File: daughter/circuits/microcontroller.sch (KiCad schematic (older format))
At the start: 17 parts, among them U13 ESP32-WROOM-32, U14 Si7020-A20

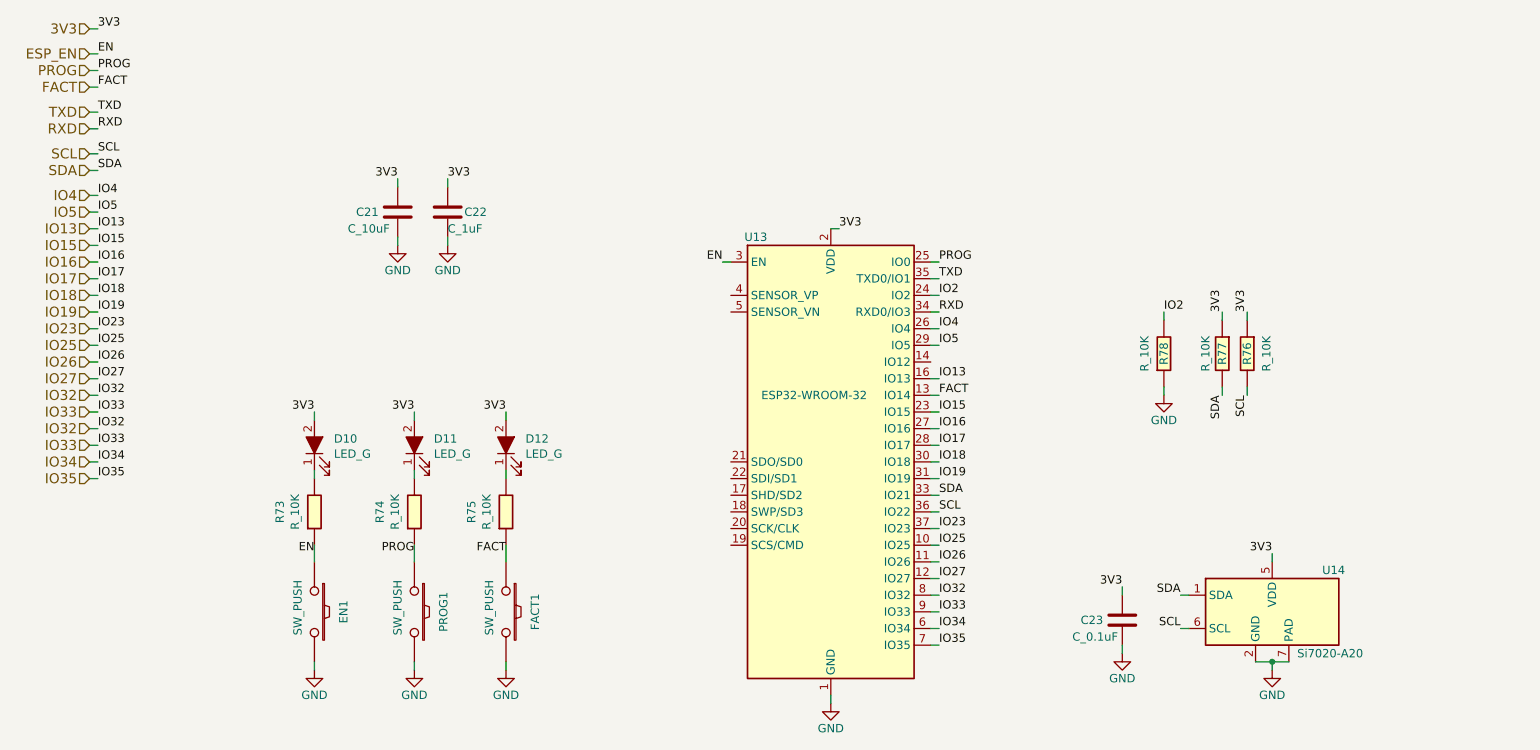
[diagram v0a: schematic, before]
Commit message: 0) Switched to h-bridge drivers for hvac 1) Connected ignition sense io 2) MCP config pins and reset 3) Fixed usb resistors 4) Fixed BJT footprint 5) Added car interface pcb for C6 Corvette
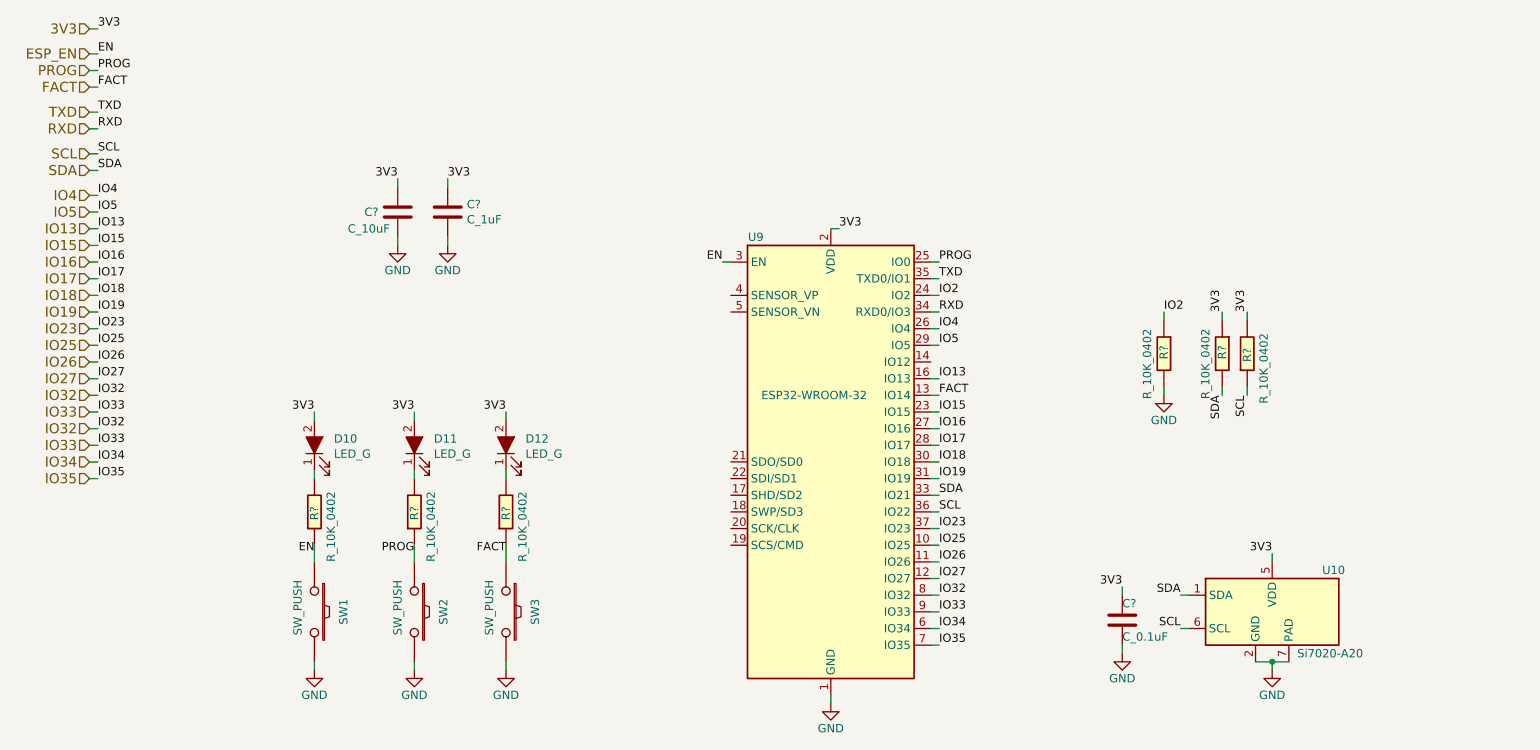
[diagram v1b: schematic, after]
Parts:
- removed C21: C_10uF, Capacitor_SMD:C_0603_1608Metric_Pad1.08x0.95mm_HandSolder, symbol open-dash-daughterboard-rescue:C_10uF-Open_Automation
- removed C22: C_1uF, Capacitor_SMD:C_0603_1608Metric_Pad1.08x0.95mm_HandSolder, symbol open-dash-daughterboard-rescue:C_1uF-Open_Automation
- removed C23: C_0.1uF, Capacitor_SMD:C_0603_1608Metric_Pad1.08x0.95mm_HandSolder, symbol open-dash-daughterboard-rescue:C_0.1uF-Open_Automation
- removed R73, R74, R75, R76, R77, R78: R_10K, Resistor_SMD:R_0603_1608Metric_Pad0.98x0.95mm_HandSolder, symbol open-dash-daughterboard-rescue:R_10K-Open_Automation
- removed U13: ESP32-WROOM-32, RF_Module:ESP32-WROOM-32, symbol open-dash-daughterboard-rescue:ESP32-WROOM-32-Open_Automation
- added C?: C_10uF, Capacitor_SMD:C_0805_2012Metric_Pad1.18x1.45mm_HandSolder, symbol Open_Automation:C_10uF
- added C?: C_1uF, Capacitor_SMD:C_0402_1005Metric_Pad0.74x0.62mm_HandSolder, symbol Open_Automation:C_1uF
- added C?: C_0.1uF, Capacitor_SMD:C_0402_1005Metric_Pad0.74x0.62mm_HandSolder, symbol Open_Automation:C_0.1uF
- added R? (x6): R_10K_0402, Resistor_SMD:R_0402_1005Metric_Pad0.72x0.64mm_HandSolder, symbol Open_Automation:R_10K_0402
- added U9: ESP32-WROOM-32, RF_Module:ESP32-WROOM-32, symbol open-dash-daughterboard-rescue:ESP32-WROOM-32-Open_Automation
- renumbered EN1 to SW1, PROG1 to SW2, FACT1 to SW3, U14 to U10
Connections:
- net 3V3: now also C?.1, C?.1, C?.1, R?.1, R?.2, U9.2 (VDD)
- net ESP_EN: now also R?.1, U9.3 (EN)
- net FACT: now also R?.1, U9.13 (IO14)
- net GND: now also C?.2, C?.2, C?.2, R?.2, U9.1 (GND), U9.15 (GND), U9.38 (GND), U9.39 (GND)
- net IO13: now also U9.16 (IO13)
- net IO15: now also U9.23 (IO15)
- net IO16: now also U9.27 (IO16)
- net IO17: now also U9.28 (IO17)
- net IO18: now also U9.30 (IO18)
- net IO19: now also U9.31 (IO19)
- net IO2: now also R?.1, U9.24 (IO2)
- net IO23: now also U9.37 (IO23)
- net IO25: now also U9.10 (IO25)
- net IO26: now also U9.11 (IO26)
- net IO27: now also U9.12 (IO27)
- net IO32: now also U9.8 (IO32)
- net IO33: now also U9.9 (IO33)
- net IO34: now also U9.6 (IO34)
- net IO35: now also U9.7 (IO35)
- net IO4: now also U9.26 (IO4)
- net IO5: now also U9.29 (IO5)
- net PROG: now also R?.1, U9.25 (IO0)
- net RXD: now also U9.34 (RXD0/IO3)
- net SCL: now also R?.1, U9.36 (IO22)
- net SDA: now also R?.2, U9.33 (IO21)
- net TXD: now also U9.35 (TXD0/IO1)
- net at D10.1 (K): now also R?.2
- net at D11.1 (K): now also R?.2
- net at D12.1 (K): now also R?.2

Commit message: finished schematic, working on layout
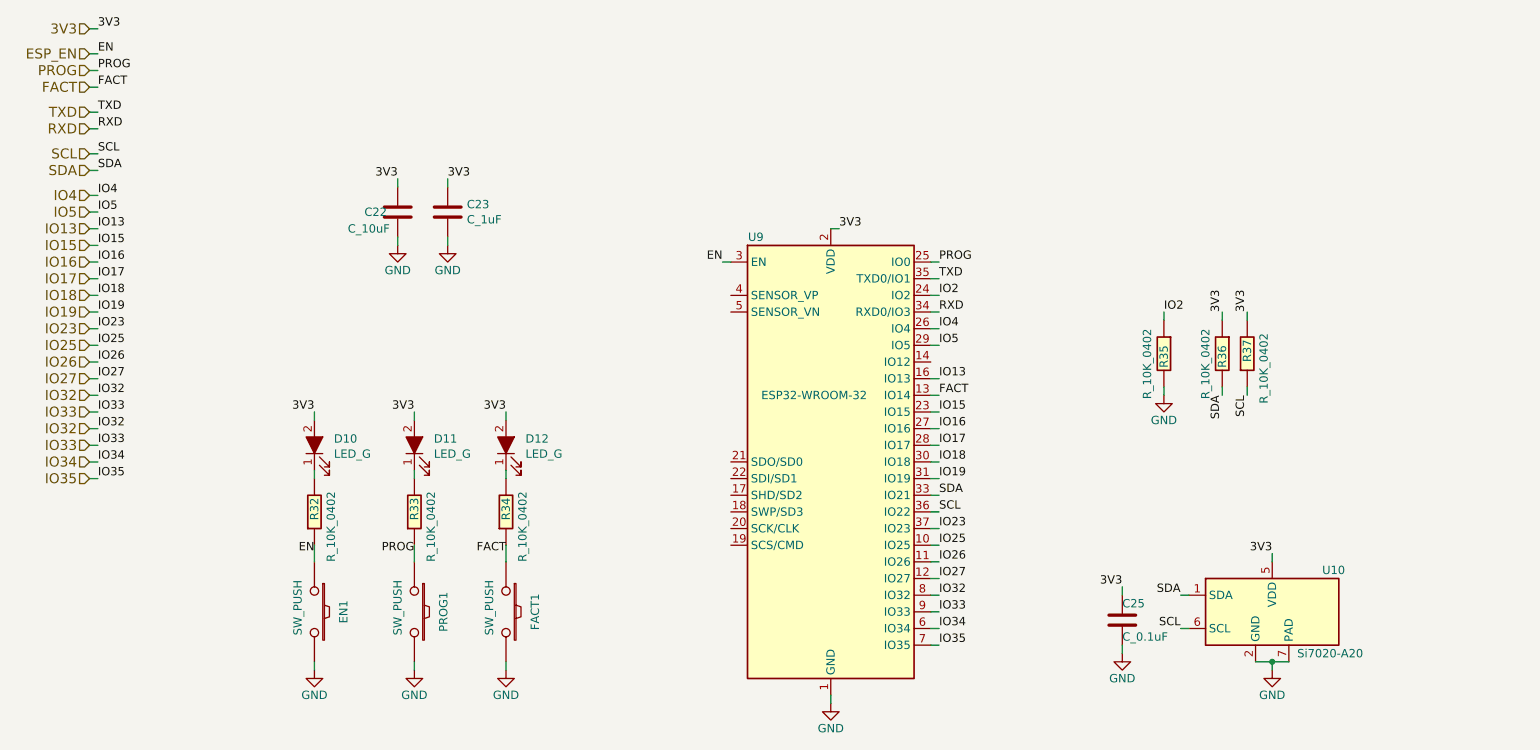
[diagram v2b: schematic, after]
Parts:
- gave numbers to parts that had none: 9
- renumbered SW1 to EN1, SW3 to FACT1, SW2 to PROG1
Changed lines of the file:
@@
 AR Path="/5ABD187E/5CC69855" Ref="SW?"  Part="1"
 AR Path="/5A7BADDB/5CC69855" Ref="SW?"  Part="1"
-AR Path="/6077D777/5CC69855" Ref="SW3"  Part="1"
-F 0 "SW3" H 3750 4625 50  0000 C CNN
+AR Path="/6077D777/5CC69855" Ref="FACT1"  Part="1"
+F 0 "FACT1" H 3750 4625 50  0000 C CNN
 F 1 "SW_PUSH" H 3725 4350 50  0000 C CNN
 F 2 "Button_Switch_SMD:SW_SPST_PTS645" H 3750 4450 50  0001 C CNN
@@
 AR Path="/5ABD187E/5CC68117" Ref="SW?"  Part="1"
 AR Path="/5A7BADDB/5CC68117" Ref="SW?"  Part="1"
-AR Path="/6077D777/5CC68117" Ref="SW2"  Part="1"
-F 0 "SW2" H 3200 4625 50  0000 C CNN
+AR Path="/6077D777/5CC68117" Ref="PROG1"  Part="1"
+F 0 "PROG1" H 3200 4625 50  0000 C CNN
 F 1 "SW_PUSH" H 3175 4350 50  0000 C CNN
 F 2 "Button_Switch_SMD:SW_SPST_PTS645" H 3200 4450 50  0001 C CNN
@@
 AR Path="/5ABD187E/5CC89C1F" Ref="SW?"  Part="1"
 AR Path="/5A7BADDB/5CC89C1F" Ref="SW?"  Part="1"
-AR Path="/6077D777/5CC89C1F" Ref="SW1"  Part="1"
-F 0 "SW1" H 2600 4625 50  0000 C CNN
+AR Path="/6077D777/5CC89C1F" Ref="EN1"  Part="1"
+F 0 "EN1" H 2600 4625 50  0000 C CNN
 F 1 "SW_PUSH" H 2575 4350 50  0000 C CNN
 F 2 "Button_Switch_SMD:SW_SPST_PTS645" H 2600 4450 50  0001 C CNN
@@
 $EndComp
 $Comp
-L Open_Automation:C_10uF C?
+L Open_Automation:C_10uF C22
 U 1 1 604C35AE
 P 3100 2050
-F 0 "C?" H 2900 2050 50  0000 L CNN
+F 0 "C22" H 2900 2050 50  0000 L CNN
 F 1 "C_10uF" H 2800 1950 50  0000 L CNN
 F 2 "Capacitor_SMD:C_0805_2012Metric_Pad1.18x1.45mm_HandSolder" H 3350 2500 50  0001 C CNN
@@
 $EndComp
 $Comp
-L Open_Automation:C_1uF C?
+L Open_Automation:C_1uF C23
 U 1 1 604D0693
 P 3400 2050
-F 0 "C?" H 3515 2096 50  0000 L CNN
+F 0 "C23" H 3515 2096 50  0000 L CNN
 F 1 "C_1uF" H 3515 2005 50  0000 L CNN
 F 2 "Capacitor_SMD:C_0402_1005Metric_Pad0.74x0.62mm_HandSolder" H 3500 2350 50  0001 C CNN
@@
 $EndComp
 $Comp
-L Open_Automation:R_10K_0402 R?
+L Open_Automation:R_10K_0402 R32
 U 1 1 604D6E5B
 P 2600 3850
-F 0 "R?" V 2600 3800 50  0000 L CNN
+F 0 "R32" V 2600 3800 50  0000 L CNN
 F 1 "R_10K_0402" V 2700 3550 50  0000 L CNN
 F 2 "Resistor_SMD:R_0402_1005Metric_Pad0.72x0.64mm_HandSolder" V 2530 3850 50  0001 C CNN
@@
 $EndComp
 $Comp
-L Open_Automation:R_10K_0402 R?
+L Open_Automation:R_10K_0402 R33
 U 1 1 604D9703
 P 3200 3850
-F 0 "R?" V 3200 3800 50  0000 L CNN
+F 0 "R33" V 3200 3800 50  0000 L CNN
 F 1 "R_10K_0402" V 3300 3550 50  0000 L CNN
 F 2 "Resistor_SMD:R_0402_1005Metric_Pad0.72x0.64mm_HandSolder" V 3130 3850 50  0001 C CNN
@@
 $EndComp
 $Comp
-L Open_Automation:R_10K_0402 R?
+L Open_Automation:R_10K_0402 R34
 U 1 1 604D9A3E
 P 3750 3850
-F 0 "R?" V 3750 3800 50  0000 L CNN
+F 0 "R34" V 3750 3800 50  0000 L CNN
 F 1 "R_10K_0402" V 3850 3550 50  0000 L CNN
 F 2 "Resistor_SMD:R_0402_1005Metric_Pad0.72x0.64mm_HandSolder" V 3680 3850 50  0001 C CNN
@@
 $EndComp
 $Comp
-L Open_Automation:R_10K_0402 R?
+L Open_Automation:R_10K_0402 R37
 U 1 1 604DD677
 P 8200 2900
-F 0 "R?" V 8200 2850 50  0000 L CNN
+F 0 "R37" V 8200 2850 50  0000 L CNN
 F 1 "R_10K_0402" V 8300 2600 50  0000 L CNN
 F 2 "Resistor_SMD:R_0402_1005Metric_Pad0.72x0.64mm_HandSolder" V 8130 2900 50  0001 C CNN
@@
 $EndComp
 $Comp
-L Open_Automation:R_10K_0402 R?
+L Open_Automation:R_10K_0402 R36
 U 1 1 604DEC4B
 P 8050 2900
-F 0 "R?" V 8050 2850 50  0000 L CNN
+F 0 "R36" V 8050 2850 50  0000 L CNN
 F 1 "R_10K_0402" V 8150 2750 50  0000 L CNN
 F 2 "Resistor_SMD:R_0402_1005Metric_Pad0.72x0.64mm_HandSolder" V 7980 2900 50  0001 C CNN
@@
 $EndComp
 $Comp
-L Open_Automation:R_10K_0402 R?
+L Open_Automation:R_10K_0402 R35
 U 1 1 604DF274
 P 7700 2900
-F 0 "R?" V 7700 2850 50  0000 L CNN
+F 0 "R35" V 7700 2850 50  0000 L CNN
 F 1 "R_10K_0402" V 7800 2750 50  0000 L CNN
 F 2 "Resistor_SMD:R_0402_1005Metric_Pad0.72x0.64mm_HandSolder" V 7630 2900 50  0001 C CNN
@@
 $EndComp
 $Comp
-L Open_Automation:C_0.1uF C?
+L Open_Automation:C_0.1uF C25
 U 1 1 604F0FE9
 P 7450 4500
-F 0 "C?" H 7450 4600 50  0000 L CNN
+F 0 "C25" H 7450 4600 50  0000 L CNN
 F 1 "C_0.1uF" H 7450 4400 50  0000 L CNN
 F 2 "Capacitor_SMD:C_0402_1005Metric_Pad0.74x0.62mm_HandSolder" H 7550 4800 50  0001 C CNN

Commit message: sent v1.2 to fab
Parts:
- removed U10: Si7020-A20, Package_DFN_QFN:DFN-6-1EP_3x3mm_P1mm_EP1.5x2.4mm, symbol open-dash-daughterboard-rescue:Si7020-A20-Sensor_Humidity
- added U10: Temp_Hum_HDC1080DMBR, Package_DFN_QFN:DFN-6-1EP_3x3mm_P1mm_EP1.5x2.4mm, symbol Open_Automation:Temp_Hum_HDC1080DMBR
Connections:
- net 3V3: now also U10.5 (VDD)
- net GND: now also U10.2 (GND), U10.7 (PAD)
- net SCL: now also U10.6 (SCL)
- net SDA: now also U10.1 (SDA)
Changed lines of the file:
@@
 	7800 4550 7850 4550
-$Comp
-L open-dash-daughterboard-rescue:Si7020-A20-Sensor_Humidity U10
-U 1 1 602D690F
-P 8350 4450
-F 0 "U10" H 8650 4700 50  0000 L CNN
-F 1 "Si7020-A20" H 8500 4200 50  0000 L CNN
-F 2 "Package_DFN_QFN:DFN-6-1EP_3x3mm_P1mm_EP1.5x2.4mm" H 8350 4050 50  0001 C CNN
-F 3 "https://datasheet.lcsc.com/szlcsc/2005151605_SILICON-LABS-SI7020-A20-GM1_C430229.pdf" H 8150 4750 50  0001 C CNN
-F 4 "SI7020-A20-GM1" H 0   0   50  0001 C CNN "Part Number"
-F 5 "C430229" H 0   0   50  0001 C CNN "LCSC"
-	1    8350 4450
-	1    0    0    -1
-$EndComp
 $Comp
 L Open_Automation:C_10uF C22
@@
 	1    0    0    -1
 $EndComp
+$Comp
+L Open_Automation:Temp_Hum_HDC1080DMBR U10
+U 1 1 6064A5B2
+P 8350 4450
+F 0 "U10" H 8794 4496 50  0000 L CNN
+F 1 "Temp_Hum_HDC1080DMBR" H 8794 4405 50  0000 L CNN
+F 2 "Package_DFN_QFN:DFN-6-1EP_3x3mm_P1mm_EP1.5x2.4mm" H 8350 5200 50  0001 C CNN
+F 3 "https://datasheet.lcsc.com/szlcsc/1810271112_Texas-Instruments-HDC1080DMBR_C82227.pdf" H 8150 4750 50  0001 C CNN
+F 4 "HDC1080DMBR" H 8650 4800 50  0001 C CNN "Part Number"
+F 5 "C82227" H 8650 4900 50  0001 C CNN "LCSC"
+	1    8350 4450
+	1    0    0    -1
+$EndComp

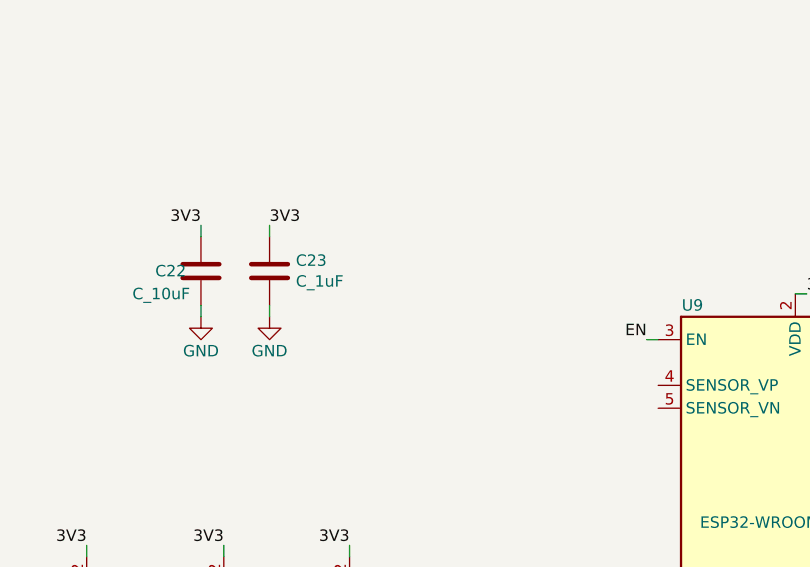
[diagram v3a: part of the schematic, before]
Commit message: Using npn-pnp high side switch for ext amp trigger.
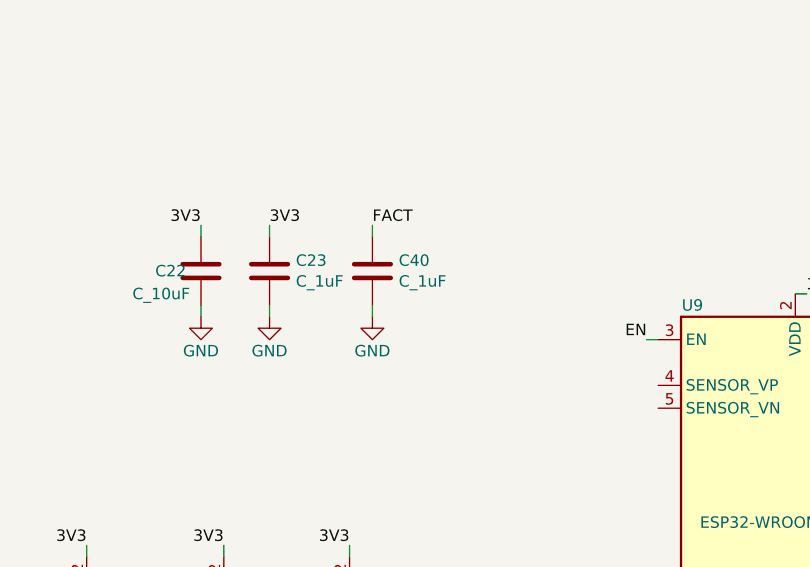
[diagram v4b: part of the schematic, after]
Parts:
- added C40: C_1uF, Capacitor_SMD:C_0402_1005Metric_Pad0.74x0.62mm_HandSolder, symbol Open_Automation:C_1uF
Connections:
- net FACT: now also C40.1
- net GND: now also C40.2
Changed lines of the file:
@@
 	1    0    0    -1
 $EndComp
+$Comp
+L open-dash-daughterboard-rescue:GND-power #PWR?
+U 1 1 61952B18
+P 3850 2250
+AR Path="/5A7BADDB/61952B18" Ref="#PWR?"  Part="1"
+AR Path="/6077D777/61952B18" Ref="#PWR0107"  Part="1"
+F 0 "#PWR0107" H 3850 2000 50  0001 C CNN
+F 1 "GND" H 3850 2100 50  0000 C CNN
+F 2 "" H 3850 2250 50  0000 C CNN
+F 3 "" H 3850 2250 50  0000 C CNN
+	1    3850 2250
+	1    0    0    -1
+$EndComp
+Wire Wire Line
+	3850 2200 3850 2250
+Wire Wire Line
+	3850 1850 3850 1900
+$Comp
+L Open_Automation:C_1uF C40
+U 1 1 61952C79
+P 3850 2050
+F 0 "C40" H 3965 2096 50  0000 L CNN
+F 1 "C_1uF" H 3965 2005 50  0000 L CNN
+F 2 "Capacitor_SMD:C_0402_1005Metric_Pad0.74x0.62mm_HandSolder" H 3950 2350 50  0001 C CNN
+F 3 "https://datasheet.lcsc.com/szlcsc/Samsung-Electro-Mechanics-CL05A105KA5NQNC_C52923.pdf" H 3850 1800 50  0001 C CNN
+F 4 "C52923" H 3850 2450 50  0001 C CNN "LCSC"
+F 5 "CL05A105KA5NQNC" H 3975 2250 60  0001 C CNN "Part Number"
+	1    3850 2050
+	1    0    0    -1
+$EndComp
+Text Label 3850 1850 0    50   ~ 0
+FACT
 $EndSCHEMATC
